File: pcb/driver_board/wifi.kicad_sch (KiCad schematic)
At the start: 11 parts, among them Q1 BF244A, U3 ATWINC1500B-MU-Y, Y3 Crystal_GND24

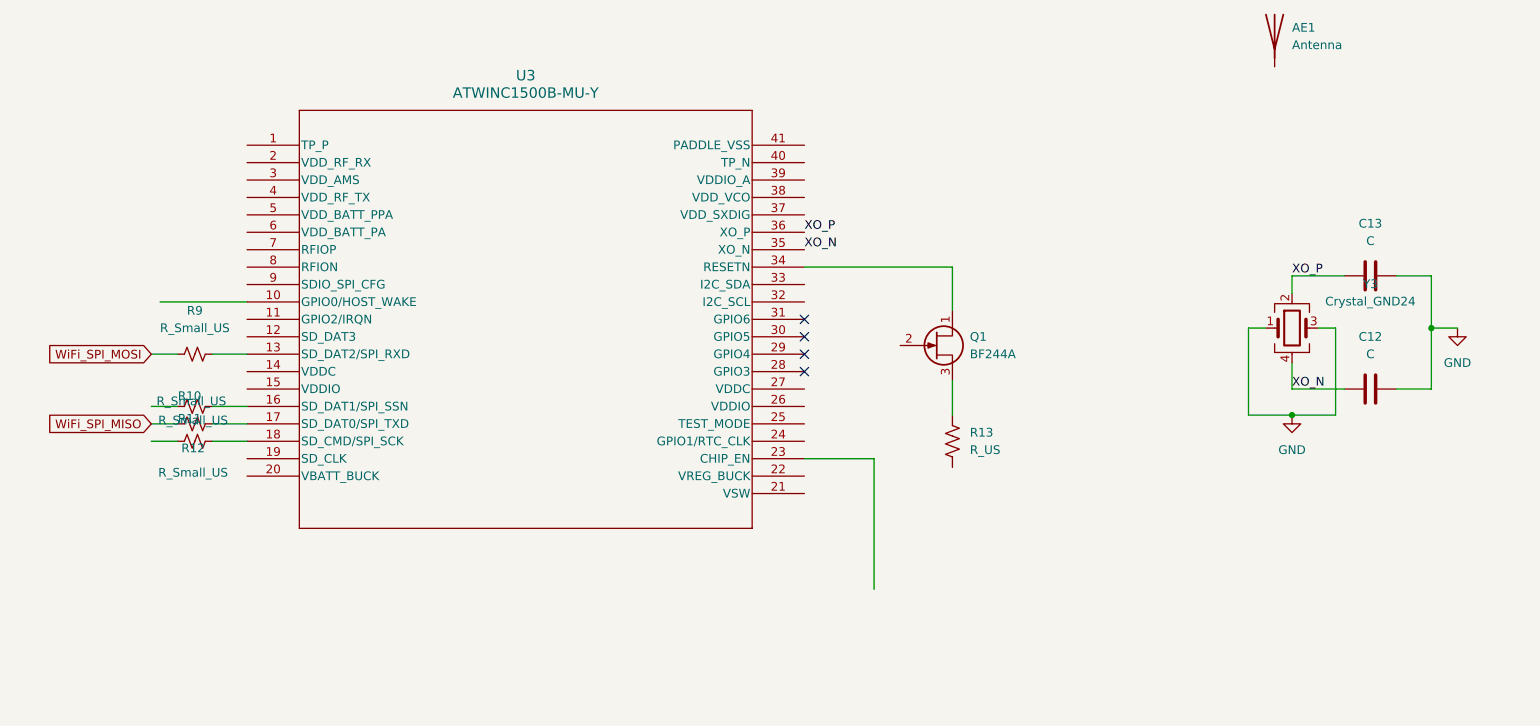
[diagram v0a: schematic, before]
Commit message: add regulators for VDDIO/VDDCORE
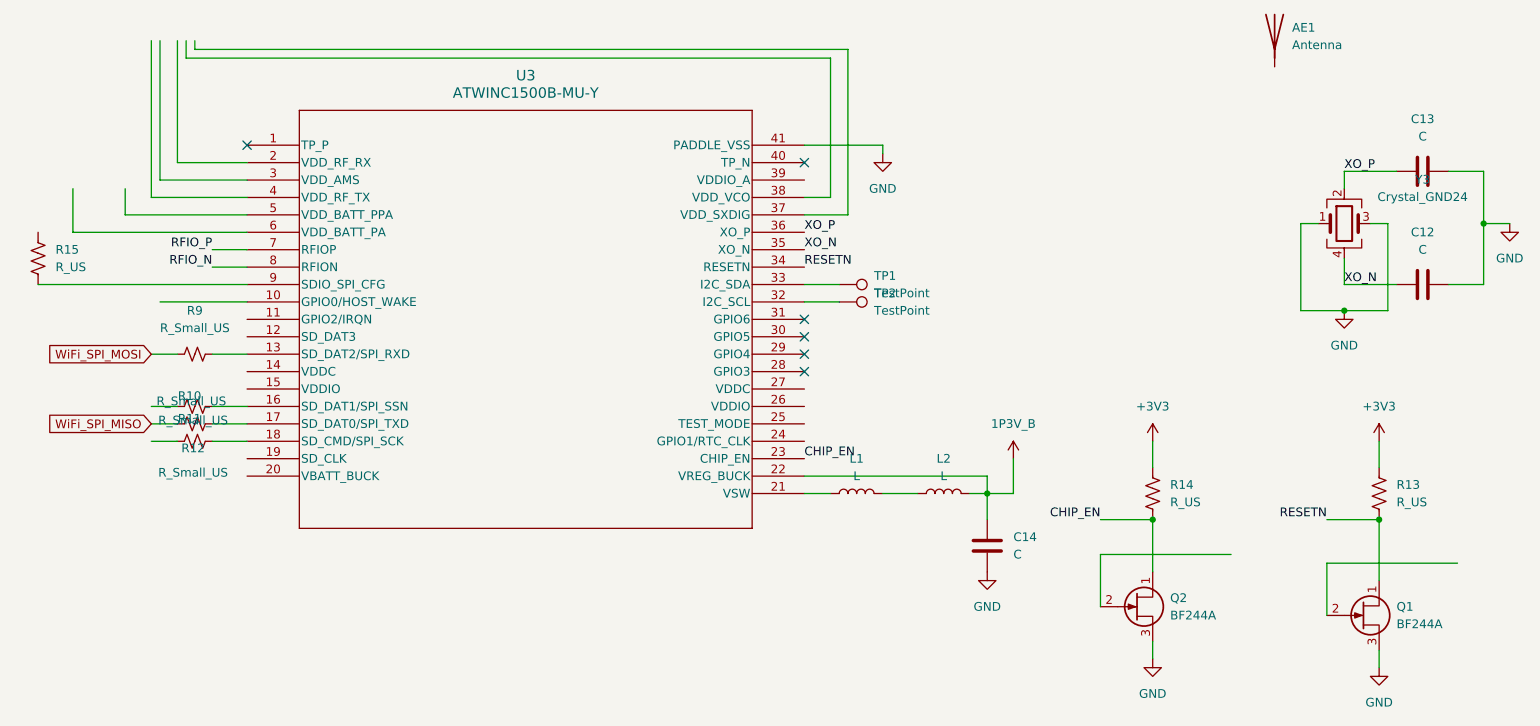
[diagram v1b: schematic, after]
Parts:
- added C14: C, symbol Device:C
- added L1, L2: L, symbol Device:L
- added Q2: BF244A, Package_TO_SOT_THT:TO-92_Inline, symbol Transistor_FET:BF244A
- added R14, R15: R_US, symbol Device:R_US
- added TP1, TP2: TestPoint, symbol Connector:TestPoint
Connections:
- net GND: now also Q1.3 (S), U3.41 (PADDLE_VSS), C14.2, Q2.3 (S)
- net RESETN: now reaches Q1.1 (D), U3.34 (RESETN)
- net RESETN: now also R13.2
- net +3V3: now reaches R13.1
- net +3V3: now also R14.1; no longer Q1.3 (S)
- net at U3.21 (VSW): now also L1.1
- net 1P3V_B: now reaches U3.22 (VREG_BUCK)
- net 1P3V_B: now also C14.1, L2.2
- net CHIP_EN: now reaches U3.23 (CHIP_EN)
- net CHIP_EN: now also Q2.1 (D), R14.2
- net at U3.32 (I2C_SCL): now also TP2.1
- net at U3.33 (I2C_SDA): now also TP1.1
- net RFIO_P: now reaches U3.7 (RFIOP)
- net RFIO_N: now reaches U3.8 (RFION)
- net at U3.9 (SDIO_SPI_CFG): now also R15.2
- new net: L1.2, L2.1
- no-connect marks 4 -> 6
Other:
- moved on the sheet: C12, C13, Q1, Y3
